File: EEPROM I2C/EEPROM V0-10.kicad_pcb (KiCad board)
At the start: 2 copper layers, 15 parts, among them K1 COLONETTE, K2 COLONETTE, K3 COLONETTE, K4 COLONETTE, P1 CONN_4, P2 CONN_4, SW1 SWITCH_X_4, U1 24C16

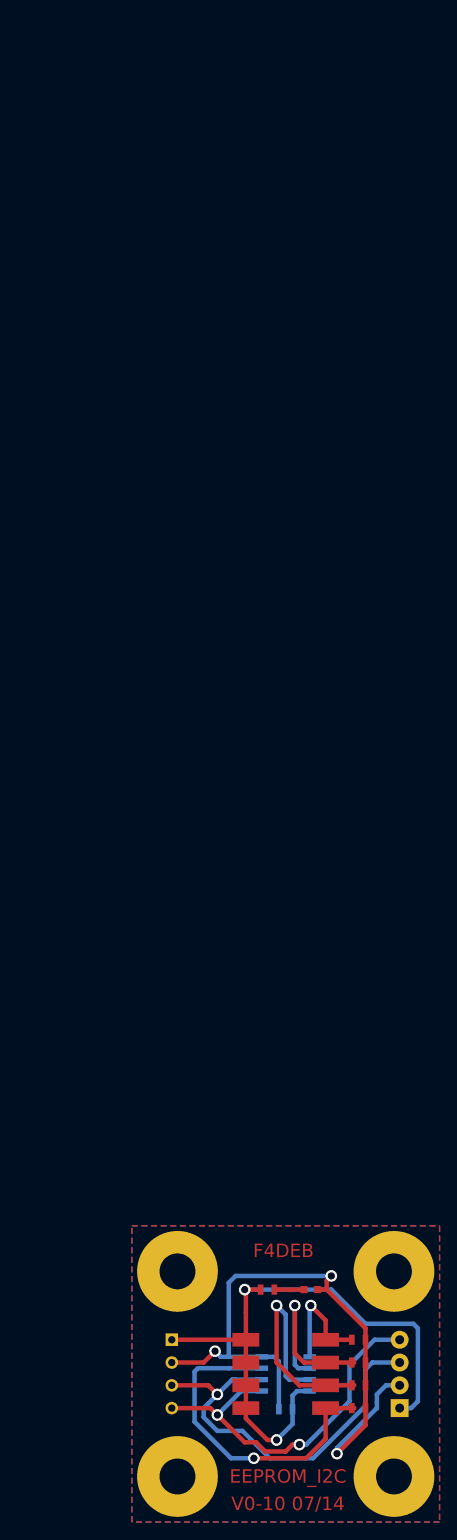
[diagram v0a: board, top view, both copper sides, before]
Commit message: Modification for printing
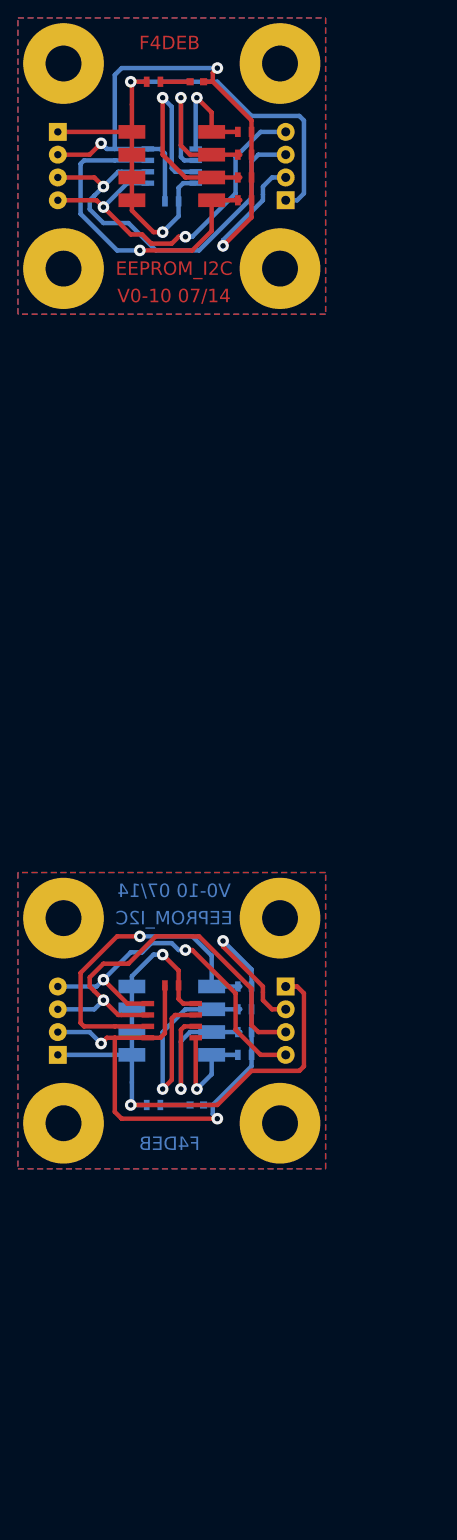
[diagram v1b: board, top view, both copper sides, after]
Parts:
- added C1: 100n, SM0603_Capa, F.Cu at (248.9, 148.5)
- added D1: VERT, LED-0603, B.Cu at (251.7, 161.8)
- added K1: COLONETTE, COLONETTE, B.Cu at (261.0, 163.8)
- added K2: COLONETTE, COLONETTE, B.Cu at (236.9, 163.8)
- added K3: COLONETTE, COLONETTE, B.Cu at (261.0, 141.0)
- added K4: COLONETTE, COLONETTE, B.Cu at (236.9, 141.0)
- added P1: CONN_4, KK-4, B.Cu at (261.6, 156.2)
- added P2: CONN_4, SIL-4, F.Cu at (236.2, 152.4)
- added R1: 1k, SM0603_Resistor, B.Cu at (246.9, 161.8)
- added R2: 10k, SM0603_Resistor, B.Cu at (257.0, 148.6)
- added R3: 10k, SM0603_Resistor, B.Cu at (257.0, 151.1)
- added R4: 10k, SM0603_Resistor, B.Cu at (257.0, 153.7)
- added R5: 10k, SM0603_Resistor, B.Cu at (257.0, 156.2)
- added SW1: SWITCH_X_4, SWCMS4, B.Cu at (248.9, 152.4)
- added U1: 24C16, SO8E, F.Cu at (248.9, 152.4)
- moved C1 135.2 mm to (248.9, 61.1)
- moved D1 135.2 mm to (251.7, 47.8)
- moved K1 135.2 mm to (261.0, 45.7)
- moved K2 135.2 mm to (236.9, 45.7)
- moved K3 135.2 mm to (261.0, 68.6)
- moved K4 135.2 mm to (236.9, 68.6)
- moved P1 135.2 mm to (261.6, 53.3)
- moved P2 135.2 mm to (236.2, 57.1)
- moved R1 135.2 mm to (246.9, 47.8)
- moved R2 135.2 mm to (257.0, 61.0)
- moved R3 135.2 mm to (257.0, 58.4)
- moved R4 135.2 mm to (257.0, 55.9)
- moved R5 135.2 mm to (257.0, 53.3)
- moved SW1 135.2 mm to (248.9, 57.1)
- moved U1 135.2 mm to (248.9, 57.1)
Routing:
- net +5VD: track 73.8 -> 147.7 mm, vias 3 -> 6
- net GND: track 68.2 -> 136.5 mm, vias 2 -> 4
- net /SCL: track 44.8 -> 89.7 mm, vias 1 -> 2
- net /SDA: track 41.0 -> 82.0 mm, vias 2 -> 4
- net /WP: track 37.3 -> 74.6 mm, vias 1 -> 2
- net N-0000011: track 27.4 -> 54.8 mm, vias 1 -> 2
- net N-0000012: track 21.0 -> 42.1 mm, vias 1 -> 2
- net N-0000013: track 13.2 -> 26.4 mm, vias 1 -> 2
- net N-000001: track 3.31 -> 6.63 mm
